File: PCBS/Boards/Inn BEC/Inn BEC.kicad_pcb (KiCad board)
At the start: 2 copper layers, 23 x 20 mm, 6 parts, among them U1 XL1509-5.0, U2 L7805

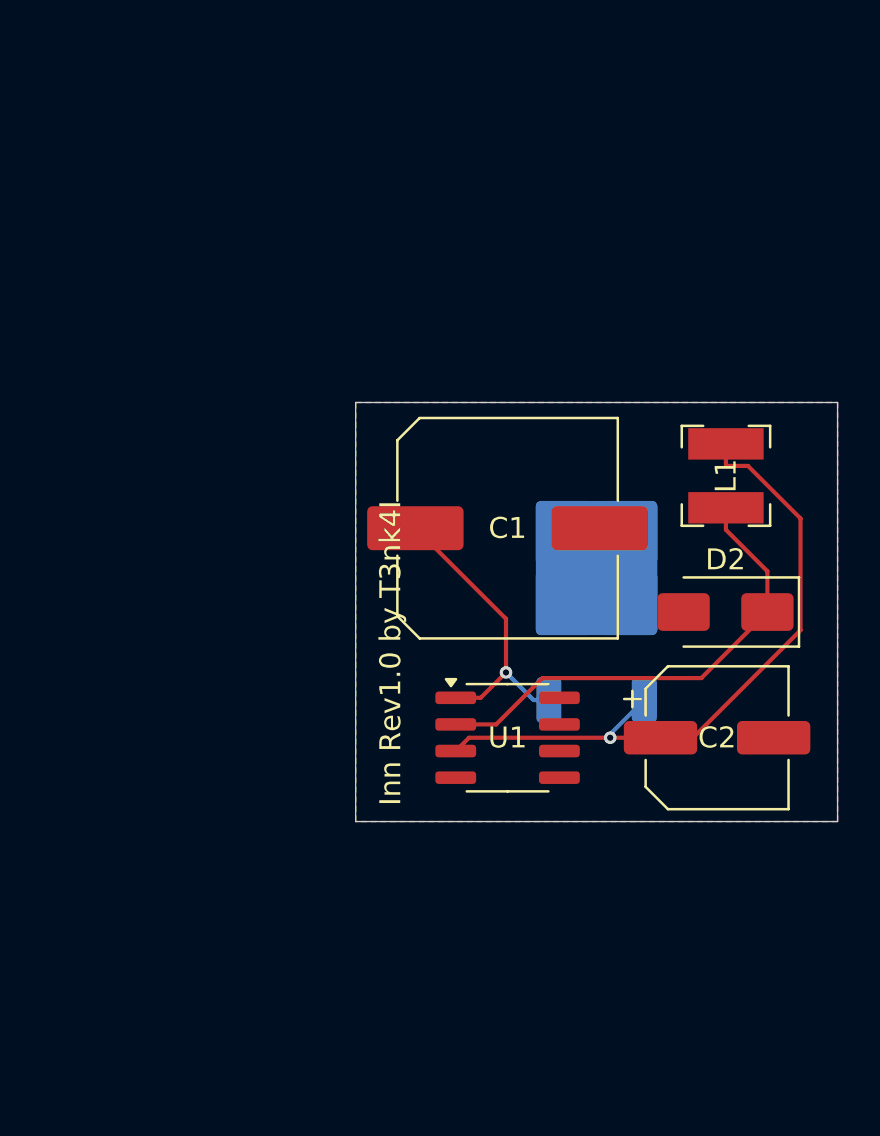
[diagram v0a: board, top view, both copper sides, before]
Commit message: updates files for INN BEC, adds production files and panelized version
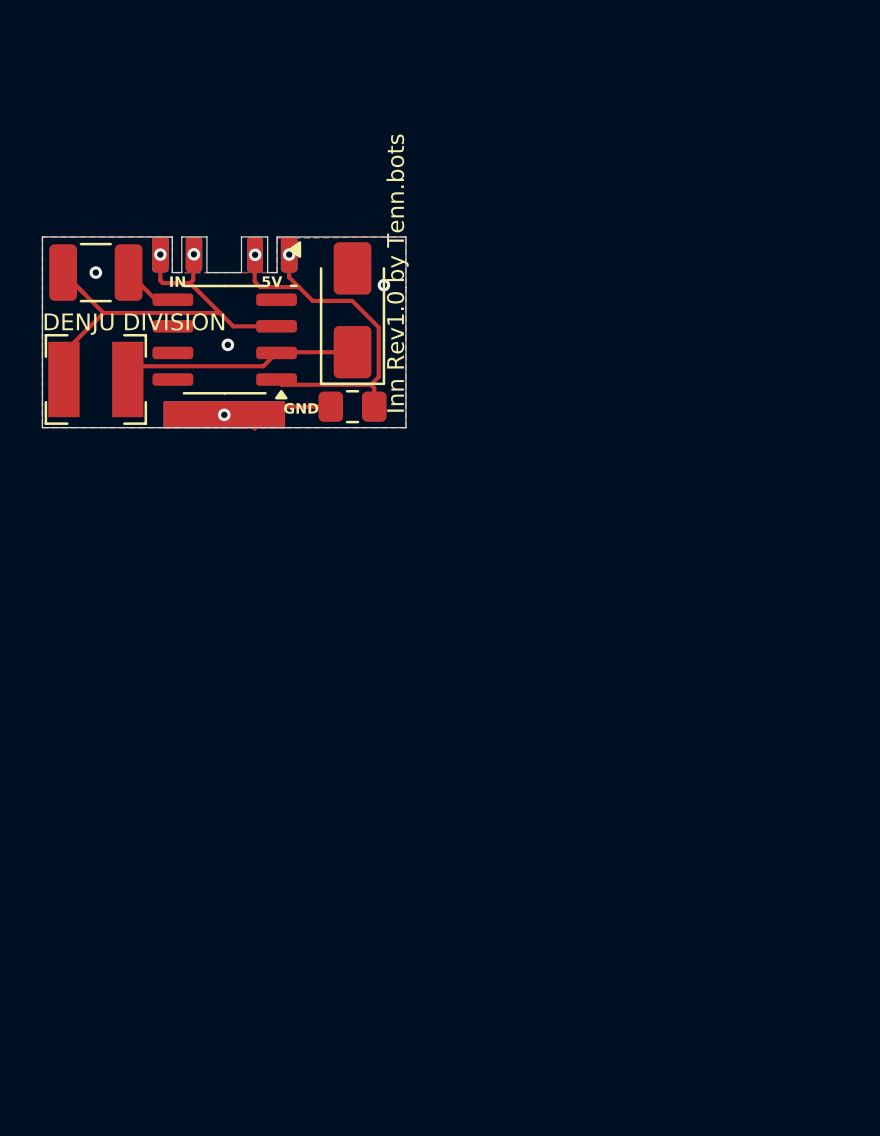
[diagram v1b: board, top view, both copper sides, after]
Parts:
- removed U2: L7805, Package_TO_SOT_SMD:TO-252-2
- added J1: Conn_01x03_Socket, Package_TO_SOT_SMD:TO-252-2, F.Cu at (142.0, 73.7)
- C1: value C -> 47uF; footprint Capacitor_SMD:C_Elec_10x10.2 -> Capacitor_SMD:C_1210_3225Metric_Pad1.33x2.70mm_HandSolder
- C2: value C_Polarized -> 22uF; footprint Capacitor_SMD:CP_Elec_6.3x7.7 -> Capacitor_SMD:C_0805_2012Metric_Pad1.18x1.45mm_HandSolder
- L1: value L -> 68uH
- moved L1 30.4 mm to (135.8, 74.9), turned to 180 degrees
- moved C2 23.5 mm to (148.1, 76.2), turned to 180 degrees
- moved U1 23.3 mm to (142.0, 73.0), turned to 180 degrees
- moved C1 23.1 mm to (135.8, 69.8)
- moved D2 22.9 mm to (148.1, 71.6), turned to 90 degrees
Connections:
- C1 pad 1: Net-(U1-VIN) -> Net-(J1-Pin_3)
- C2 pad 1: Net-(U1-FB) -> Net-(J1-Pin_1)
- L1 pad 2: Net-(U1-FB) -> Net-(J1-Pin_3)
- U1 pad 1: Net-(U1-VIN) -> Net-(J1-Pin_1)
- U1 pad 3: Net-(U1-FB) -> Net-(J1-Pin_3)
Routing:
- net Net-(U1-FB): track 32.3 -> 0.00 mm, vias 1 -> 0
- net Net-(J1-Pin_3): track 0.00 -> 22.7 mm, vias 0 -> 2
- net Net-(J1-Pin_1): track 0.00 -> 18.6 mm, vias 0 -> 2
- net Net-(U1-VIN): track 14.2 -> 0.00 mm, vias 1 -> 0
- net Net-(D2-K): track 22.9 -> 11.3 mm
- net GND: track 0.00 -> 6.71 mm, vias 0 -> 4
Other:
- board size 23 x 20 mm -> 17.3 x 9.1 mm
- board text added: "5V"
- board text added: "DENJU DIVISION"
- board text added: "GND"
- board text added: "IN"
- board text added: "Inn Rev1.0 by Tenn.bots"
- board text removed: "Inn Rev1.0 by T3nk4I"

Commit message: updated readme and PCB files
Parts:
- added G***: LOGO, LOGO, B.Cu at (150.0, 100.0)
- added J2: Conn_01x02_Pin, Connector_Wire:SolderWire-0.1sqmm_1x02_P3.6mm_D0.4mm_OD1mm, F.Cu at (148.2, 108.2)
- J1: value Conn_01x03_Socket -> Conn_01x02_Pin; footprint Package_TO_SOT_SMD:TO-252-2 -> Connector_Wire:SolderWire-0.1sqmm_1x02_P3.6mm_D0.4mm_OD1mm
- moved L1 32.3 mm to (148.2, 104.7)
- moved D1 28.9 mm to (153.7, 100.0)
- moved C2 28.1 mm to (147.3, 95.4), turned to 180 degrees
- moved U1 27.5 mm to (148.2, 99.7)
- moved J1 20.0 mm to (148.2, 92.8), turned to 0 degrees
- moved C1 19.9 mm to (153.3, 95.4)
- renumbered C2 to C1, C1 to C2, D2 to D1
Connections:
- C1 pad 1: Net-(J1-Pin_1) -> Net-(J1-Pin_2)
- C2 pad 1: Net-(J1-Pin_3) -> Net-(J2-Pin_1)
- J1 pad 1: Net-(J1-Pin_1) -> GND
- J1 pad 2: GND -> Net-(J1-Pin_2)
- L1 pad 2: Net-(J1-Pin_3) -> Net-(J2-Pin_1)
- U1 pad 1: Net-(J1-Pin_1) -> Net-(J1-Pin_2)
- U1 pad 3: Net-(J1-Pin_3) -> Net-(J2-Pin_1)
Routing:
- net Net-(J1-Pin_3): track 22.7 -> 0.00 mm, vias 2 -> 0
- net Net-(J1-Pin_1): track 18.6 -> 0.00 mm, vias 2 -> 0
- net Net-(J2-Pin_1): track 0.00 -> 16.6 mm
- net Net-(J1-Pin_2): track 0.00 -> 11.7 mm, vias 0 -> 1
- net GND: track 6.71 -> 3.16 mm, vias 4 -> 0
- net Net-(D1-K): track 11.3 -> 7.90 mm
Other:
- board size 17.3 x 9.1 mm -> 11 x 17 mm
- board text added: "Inn Rev2.0 by Tenn.bots"
- board text removed: "DENJU DIVISION"
- board text removed: "Inn Rev1.0 by Tenn.bots"
